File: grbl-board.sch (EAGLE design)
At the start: 20 parts, among them IC1 MEGA8-P, IC2 FT232RL, IC3 ADUM1250, Q1 16 MHz, X1 PN61729-S, X2 22-23-2031, X3 22-23-2031, X4 22-23-2031, X5 22-23-2021

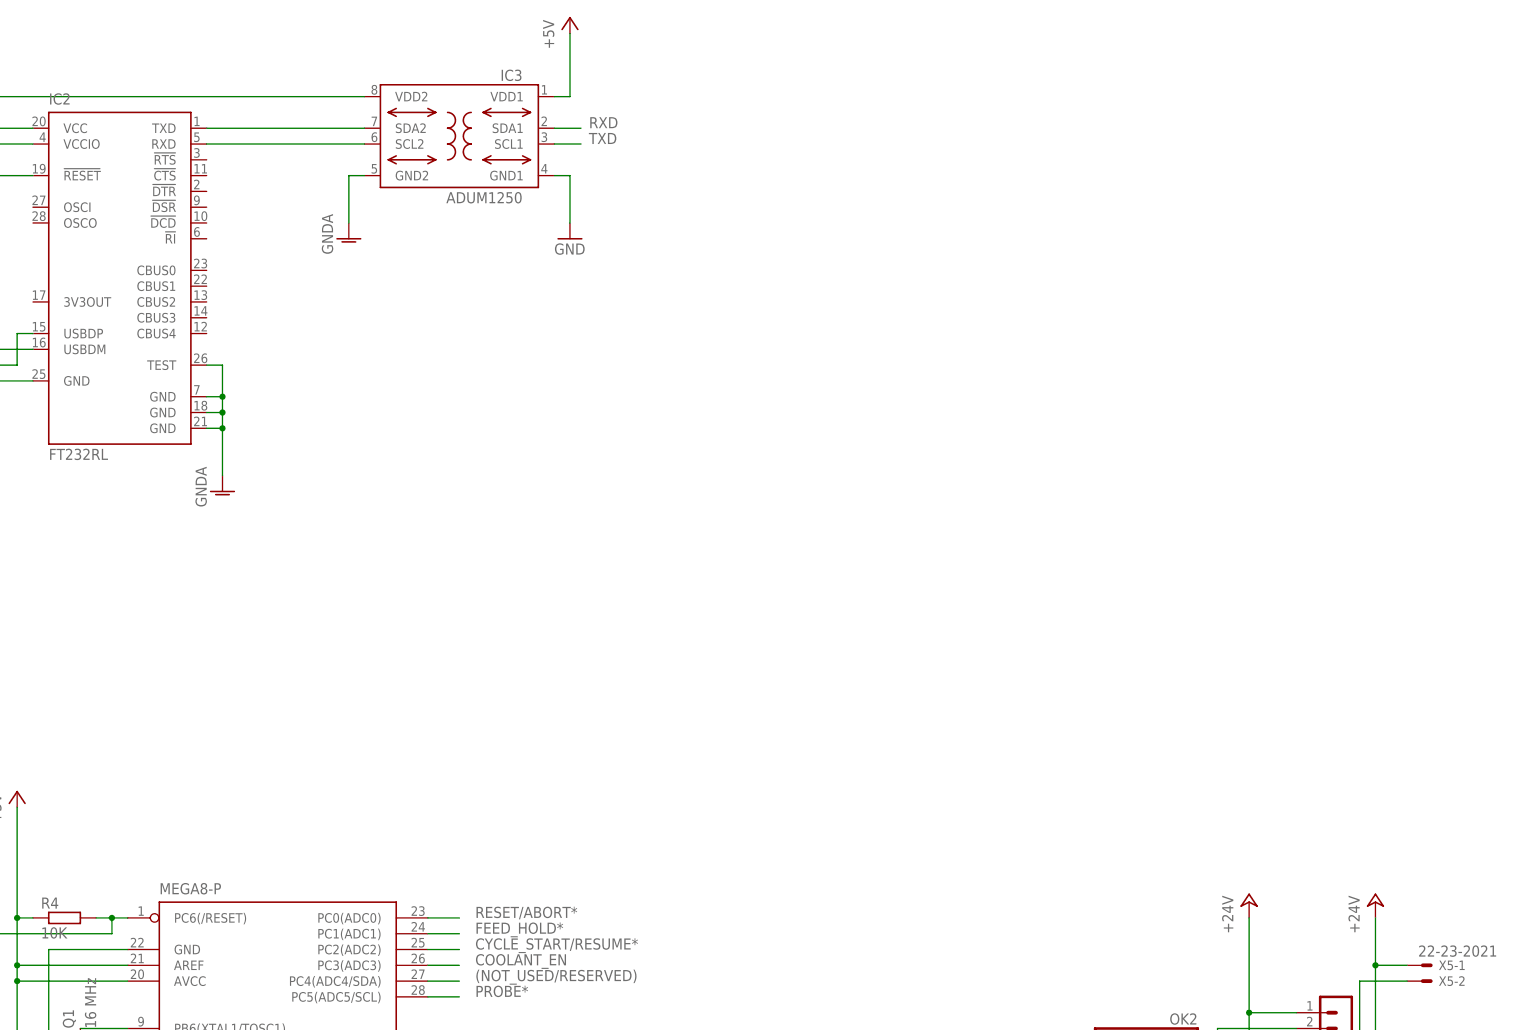
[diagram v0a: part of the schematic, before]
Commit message: add arduino nano2
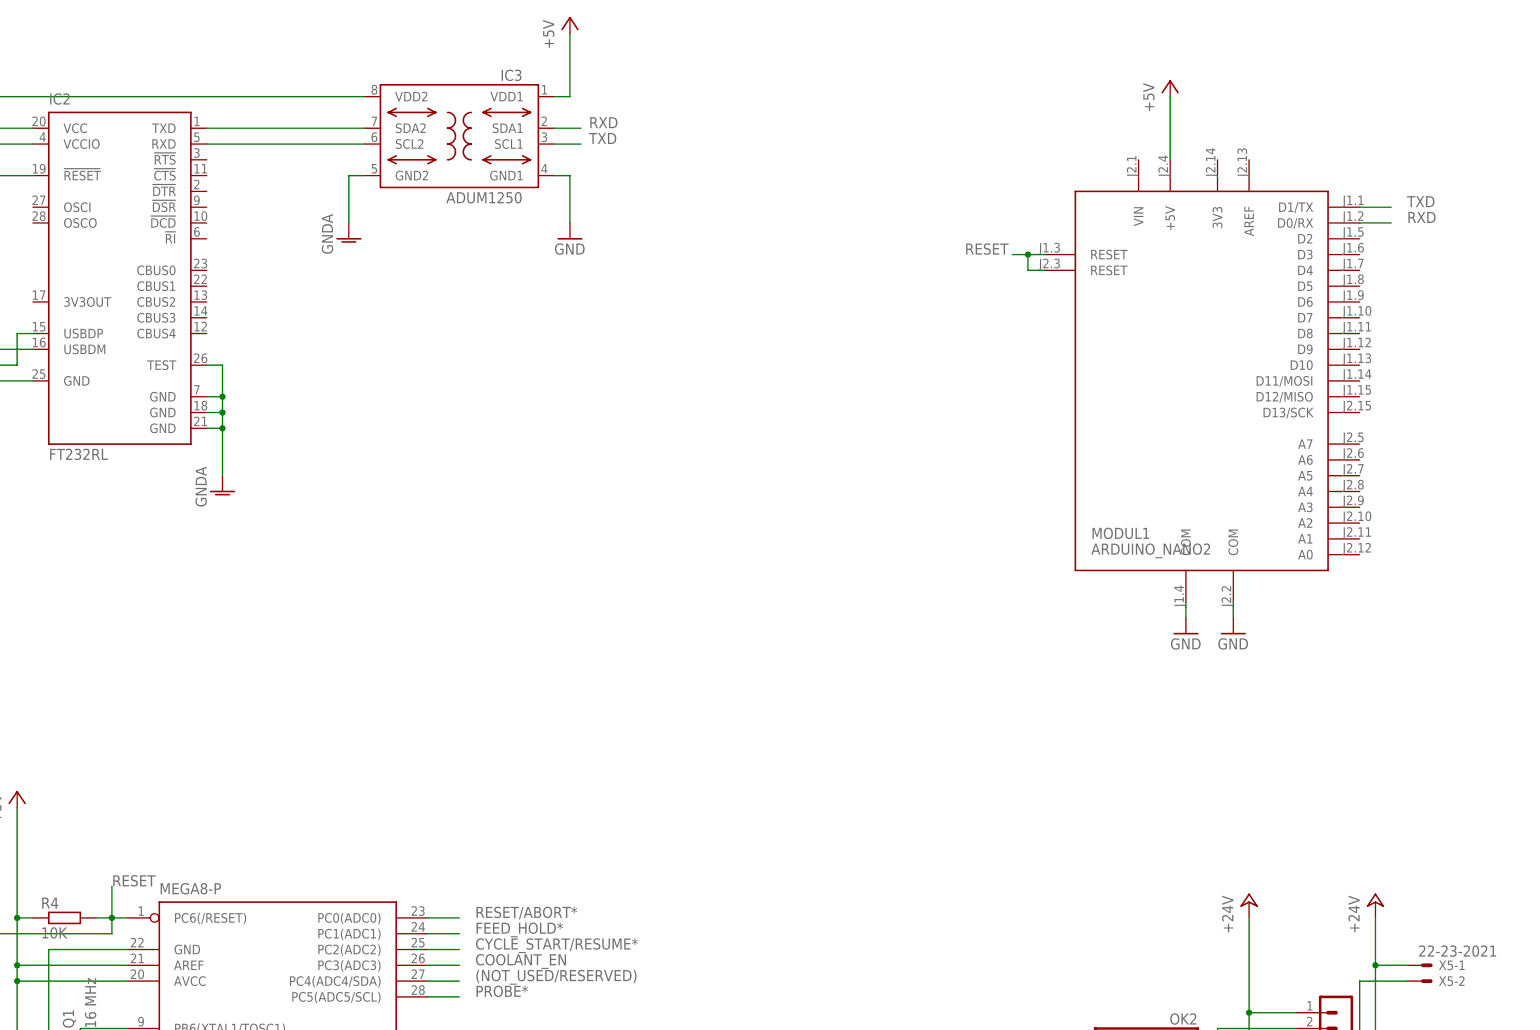
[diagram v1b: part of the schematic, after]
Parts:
- added MODUL1: ARDUINO_NANO2, arduino:ARDUINO_NANO2
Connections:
- removed net N$16: IC1.PC6(/RESET), R4.2, S1.S
- new net RESET: IC1.PC6(/RESET), MODUL1.RESET, MODUL1.RESET@2, R4.2, S1.S
- net +5V: now also MODUL1.+5V
- net GND: now also MODUL1.COM, MODUL1.COM@1
- net RXD: now also MODUL1.D0/RX
- net TXD: now also MODUL1.D1/TX
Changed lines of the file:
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@@
 <part name="S1" library="switch-omron" deviceset="10-XX" device=""/>
 <part name="GND7" library="supply1" deviceset="GND" device=""/>
+<part name="MODUL1" library="arduino" deviceset="ARDUINO_NANO2" device=""/>
+<part name="P+5" library="supply1" deviceset="+5V" device=""/>
+<part name="GND8" library="supply1" deviceset="GND" device=""/>
+<part name="GND9" library="supply1" deviceset="GND" device=""/>
 </parts>
 <sheets>
@@
 <instance part="S1" gate="1" x="81.28" y="91.44"/>
 <instance part="GND7" gate="1" x="81.28" y="53.34"/>
+<instance part="MODUL1" gate="MODUL" x="276.86" y="208.28"/>
+<instance part="P+5" gate="1" x="271.78" y="256.54"/>
+<instance part="GND8" gate="1" x="274.32" y="167.64"/>
+<instance part="GND9" gate="1" x="281.94" y="167.64"/>
 </instances>
 <busses>
@@
 <label x="160.02" y="99.06" size="1.778" layer="95"/>
 </segment>
+<segment>
+<pinref part="MODUL1" gate="MODUL" pin="D0/RX"/>
+<wire x1="302.26" y1="233.68" x2="307.34" y2="233.68" width="0.1524" layer="91"/>
+<label x="309.88" y="233.68" size="1.778" layer="95"/>
+</segment>
 </net>
 <net name="TXD" class="0">
@@
 <wire x1="152.4" y1="96.52" x2="157.48" y2="96.52" width="0.1524" layer="91"/>
 <label x="160.02" y="96.52" size="1.778" layer="95"/>
+</segment>
+<segment>
+<pinref part="MODUL1" gate="MODUL" pin="D1/TX"/>
+<wire x1="302.26" y1="236.22" x2="307.34" y2="236.22" width="0.1524" layer="91"/>
+<label x="309.88" y="236.22" size="1.778" layer="95"/>
 </segment>
 </net>
@@
 <wire x1="81.28" y1="86.36" x2="81.28" y2="55.88" width="0.1524" layer="91"/>
 <pinref part="GND7" gate="1" pin="GND"/>
+</segment>
+<segment>
+<pinref part="MODUL1" gate="MODUL" pin="COM"/>
+<wire x1="274.32" y1="172.72" x2="274.32" y2="170.18" width="0.1524" layer="91"/>
+<pinref part="GND8" gate="1" pin="GND"/>
+</segment>
+<segment>
+<pinref part="MODUL1" gate="MODUL" pin="COM@1"/>
+<wire x1="281.94" y1="172.72" x2="281.94" y2="170.18" width="0.1524" layer="91"/>
+<pinref part="GND9" gate="1" pin="GND"/>
 </segment>
 </net>
@@
 <junction x="86.36" y="121.92"/>
 </segment>
+<segment>
+<pinref part="MODUL1" gate="MODUL" pin="+5V"/>
+<pinref part="P+5" gate="1" pin="+5V"/>
+<wire x1="271.78" y1="243.84" x2="271.78" y2="254" width="0.1524" layer="91"/>
+</segment>
 </net>
 <net name="Z-LIMIT*" class="0">
@@
 </segment>
 </net>
-<net name="N$16" class="0">
+<net name="RESET" class="0">
+<segment>
+<pinref part="MODUL1" gate="MODUL" pin="RESET"/>
+<wire x1="251.46" y1="228.6" x2="248.92" y2="228.6" width="0.1524" layer="91"/>
+<pinref part="MODUL1" gate="MODUL" pin="RESET@2"/>
+<wire x1="248.92" y1="228.6" x2="246.38" y2="228.6" width="0.1524" layer="91"/>
+<wire x1="251.46" y1="226.06" x2="248.92" y2="226.06" width="0.1524" layer="91"/>
+<wire x1="248.92" y1="226.06" x2="248.92" y2="228.6" width="0.1524" layer="91"/>
+<junction x="248.92" y="228.6"/>
+<label x="238.76" y="228.6" size="1.778" layer="95"/>
+</segment>
 <segment>
 <pinref part="IC1" gate="G$1" pin="PC6(/RESET)"/>
@@
 <wire x1="81.28" y1="119.38" x2="81.28" y2="96.52" width="0.1524" layer="91"/>
 <junction x="101.6" y="121.92"/>
-</segment>
-</net>
+<label x="101.6" y="127" size="1.778" layer="95"/>
+<wire x1="101.6" y1="121.92" x2="101.6" y2="127" width="0.1524" layer="91"/>
+</segment>
+</net>

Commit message: add driver connectors
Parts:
- added X6, X7, X8: 22-23-2051, con-molex:22-23-2051
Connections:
- removed net STEPPER_ON/OFF: IC1.PB0(ICP)
- new net STEPPER_EN: IC1.PB0(ICP), MODUL1.D8, X6-5.S, X7-5.S, X8-5.S
- net (NOT_USED/RESERVED): now also MODUL1.A4
- net +5V: now also MODUL1.AREF, R4.2, X6-1.S, X7-1.S, X8-1.S; no longer R4.1
- net COOLANT_EN: now also MODUL1.A3
- net CYCLE_START/RESUME*: now also MODUL1.A2
- net FEED_HOLD*: now also MODUL1.A1
- net GND: now also X6-2.S, X7-2.S, X8-2.S
- net PROBE*: now also MODUL1.A5
- net RESET: now also R4.1; no longer R4.2
- net RESET/ABORT*: now also MODUL1.A0
- net SPINDLE-DIR: now also MODUL1.D13/SCK
- net SPINDLE-PWM: now also MODUL1.D11/MOSI
- net X-DIR: now also MODUL1.D5, X6-4.S
- net X-LIMIT*: now also MODUL1.D9
- net X-STEP: now also MODUL1.D2, X6-3.S
- net Y-DIR: now also MODUL1.D6, X7-4.S
- net Y-LIMIT*: now also MODUL1.D10
- net Y-STEP: now also MODUL1.D3, X7-3.S
- net Z-DIR: now also MODUL1.D7, X8-4.S
- net Z-LIMIT*: now also MODUL1.D12/MISO
- net Z-STEP: now also MODUL1.D4, X8-3.S
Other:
- moved on the sheet: OK1, OK2, OK3, Q1, R1, R2, R3, R4, S1, SV1, SV2, SV3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

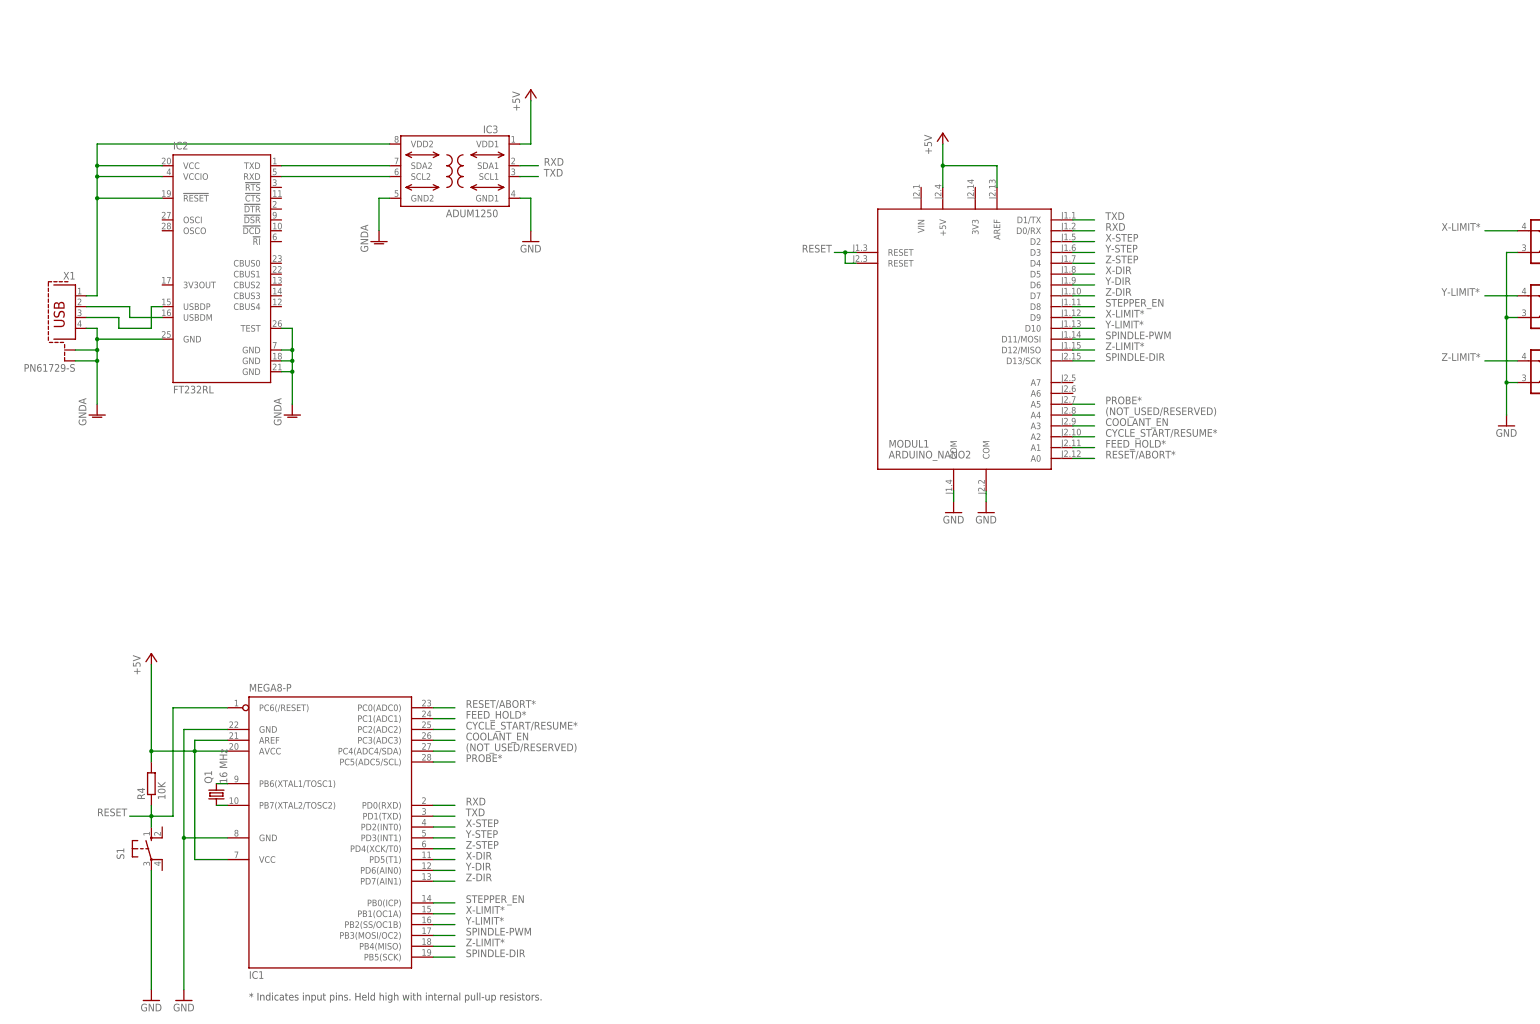
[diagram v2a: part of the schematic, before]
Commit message: add vreg add ISP
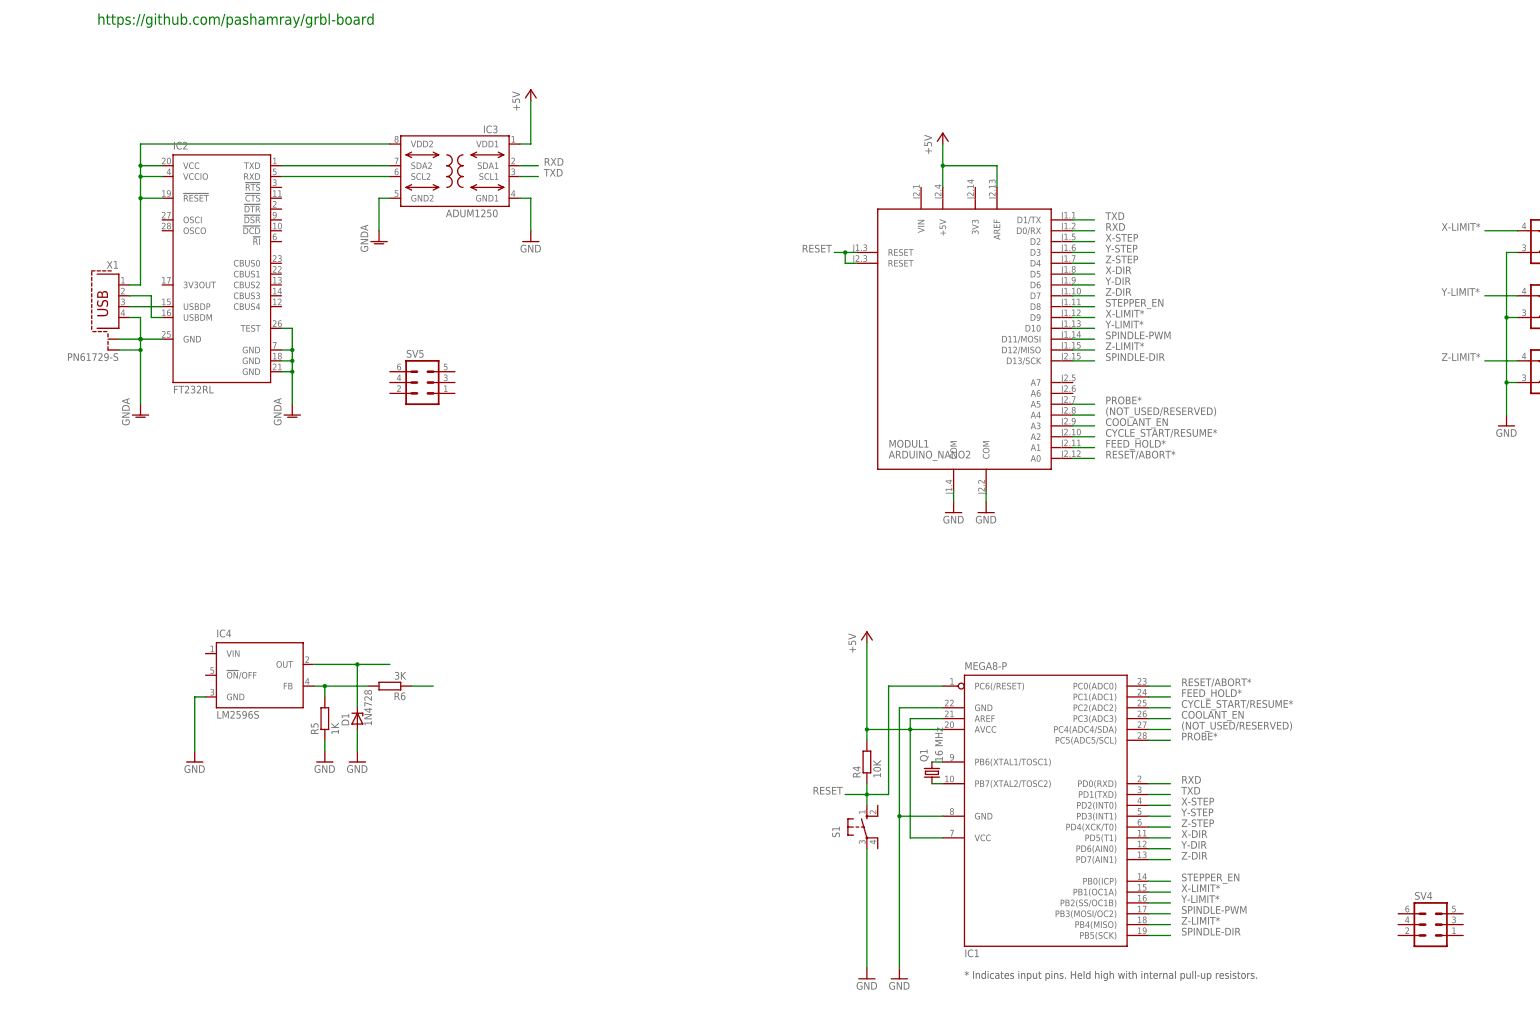
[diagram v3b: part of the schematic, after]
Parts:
- added D1: 1N4728, diode:1N4728
- added IC4: LM2596S, national-semiconductor:LM2596S
- added R5: 1K, resistor:R-EU_M0805
- added R6: 3K, resistor:R-EU_M0805
- added SV4, SV5: (no value), con-ml:ML6
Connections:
- new net N$16: D1.C, IC4.OUT
- new net N$17: R6.1
- new net N$18: IC4.FB, R5.2, R6.2
- net GND: now also D1.A, IC4.GND, R5.1
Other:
- note added: "https://github.com/pashamray/grbl-board"
- moved on the sheet: IC1, Q1, R4, S1, X1

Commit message: add arduino from adafruit library
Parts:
- removed MODUL1: ARDUINO_NANO2, arduino:ARDUINO_NANO2
- added C1: 100uF, adafruit:CPOL-USE5-13
- added C2: 1000uF, adafruit:CPOL-USE5-13
- added CN1: (no value), adafruit:DCBARRELPTH
- added L1: 100uH, adafruit:L1800R
- added U$1: ARDUINOMICRO, adafruit:ARDUINOMICRO
- D1: value 1N4728 -> 1N5822; device diode:1N4728 -> SwK-SparkFun:DIODE-SCHOTTKY_
- SV4: value (none) -> ISP
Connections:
- removed net N$17: R6.1
- new net N$19: C1.+, CN1.PWR, IC4.VIN
- net (NOT_USED/RESERVED): now also U$1.A4; no longer MODUL1.A4
- net +5V: now also C2.+, L1.1, R6.1, SV4.2, U$1.5V, U$1.AREF; no longer MODUL1.+5V, MODUL1.AREF
- net COOLANT_EN: now also U$1.A3; no longer MODUL1.A3
- net CYCLE_START/RESUME*: now also U$1.A2; no longer MODUL1.A2
- net FEED_HOLD*: now also U$1.A1; no longer MODUL1.A1
- net GND: now also C1.-, C2.-, CN1.GND, IC4.!ON!/OFF, SV4.6, U$1.GND, U$1.GND@1; no longer MODUL1.COM, MODUL1.COM@1
- net GNDA: now also SV5.6
- net N$16: now also L1.2
- net PROBE*: now also U$1.A5; no longer MODUL1.A5
- net RESET: now also SV4.5, U$1.R@1, U$1.R@2; no longer MODUL1.RESET, MODUL1.RESET@2
- net RESET/ABORT*: now also U$1.A0; no longer MODUL1.A0
- net RXD: now also U$1.RX; no longer MODUL1.D0/RX
- net SPINDLE-DIR: now also SV4.3, U$1.13; no longer MODUL1.D13/SCK
- net SPINDLE-PWM: now also SV4.4, U$1.11; no longer MODUL1.D11/MOSI
- net STEPPER_EN: now also U$1.8; no longer MODUL1.D8
- net TXD: now also U$1.TX; no longer MODUL1.D1/TX
- net X-DIR: now also U$1.5; no longer MODUL1.D5
- net X-LIMIT*: now also U$1.9; no longer MODUL1.D9
- net X-STEP: now also U$1.2; no longer MODUL1.D2
- net Y-DIR: now also U$1.6; no longer MODUL1.D6
- net Y-LIMIT*: now also U$1.10; no longer MODUL1.D10
- net Y-STEP: now also U$1.3; no longer MODUL1.D3
- net Z-DIR: now also U$1.7; no longer MODUL1.D7
- net Z-LIMIT*: now also SV4.1, U$1.12; no longer MODUL1.D12/MISO
- net Z-STEP: now also U$1.4; no longer MODUL1.D4
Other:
- moved on the sheet: IC1, IC4, OK1, OK2, OK3, Q1, R1, R2, R3, R4, R5, R6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

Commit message: add brd
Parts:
- removed IC1: MEGA8-P, atmel:MEGA8-P
- removed Q1: 16 MHz, crystal:CRYSTALHC49S
- removed R4: 10K, resistor:R-EU_M0805
- removed S1: (no value), switch-omron:10-XX
- removed SV5: (no value), con-ml:ML6
- removed X2, X3, X4: 22-23-2031, con-molex:22-23-2031
- removed X6, X7, X8: 22-23-2051, con-molex:22-23-2051
- added X-DRIVER, Y-DRIVER, Z-DRIVER: 22-23-2051, con-molex:22-23-2051
- added X-LIMIT, Y-LIMIT, Z-LIMIT: 22-23-2031, con-molex:22-23-2031
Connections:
- removed net N$6: IC1.PB6(XTAL1/TOSC1), Q1.2
- removed net N$7: IC1.PB7(XTAL2/TOSC2), Q1.1
- net (NOT_USED/RESERVED): no longer IC1.PC4(ADC4/SDA)
- net +24V: now also X-LIMIT-1.S, Y-LIMIT-1.S, Z-LIMIT-1.S; no longer X2-1.S, X3-1.S, X4-1.S
- net +5V: now also X-DRIVER-1.S, Y-DRIVER-1.S, Z-DRIVER-1.S; no longer IC1.AREF, IC1.AVCC, IC1.VCC@1, R4.2, X6-1.S, X7-1.S, X8-1.S
- net COOLANT_EN: no longer IC1.PC3(ADC3)
- net CYCLE_START/RESUME*: no longer IC1.PC2(ADC2)
- net DGND: now also X-LIMIT-3.S, Y-LIMIT-3.S, Z-LIMIT-3.S; no longer X2-3.S, X3-3.S, X4-3.S
- net FEED_HOLD*: no longer IC1.PC1(ADC1)
- net GND: now also X-DRIVER-2.S, Y-DRIVER-2.S, Z-DRIVER-2.S; no longer IC1.GND, IC1.GND@1, S1.P, X6-2.S, X7-2.S, X8-2.S
- net GNDA: no longer SV5.6
- net N$13: now also X-LIMIT-2.S; no longer X2-2.S
- net N$8: now also Y-LIMIT-2.S; no longer X3-2.S
- net N$9: now also Z-LIMIT-2.S; no longer X4-2.S
- net PROBE*: no longer IC1.PC5(ADC5/SCL)
- net RESET: no longer IC1.PC6(/RESET), R4.1, S1.S
- net RESET/ABORT*: no longer IC1.PC0(ADC0)
- net RXD: no longer IC1.PD0(RXD)
- net SPINDLE-DIR: no longer IC1.PB5(SCK)
- net SPINDLE-PWM: no longer IC1.PB3(MOSI/OC2)
- net STEPPER_EN: now also X-DRIVER-5.S, Y-DRIVER-5.S, Z-DRIVER-5.S; no longer IC1.PB0(ICP), X6-5.S, X7-5.S, X8-5.S
- net TXD: no longer IC1.PD1(TXD)
- net X-DIR: now also X-DRIVER-4.S; no longer IC1.PD5(T1), X6-4.S
- net X-LIMIT*: no longer IC1.PB1(OC1A)
- net X-STEP: now also X-DRIVER-3.S; no longer IC1.PD2(INT0), X6-3.S
- net Y-DIR: now also Y-DRIVER-4.S; no longer IC1.PD6(AIN0), X7-4.S
- net Y-LIMIT*: no longer IC1.PB2(SS/OC1B)
- net Y-STEP: now also Y-DRIVER-3.S; no longer IC1.PD3(INT1), X7-3.S
- net Z-DIR: now also Z-DRIVER-4.S; no longer IC1.PD7(AIN1), X8-4.S
- net Z-LIMIT*: no longer IC1.PB4(MISO)
- net Z-STEP: now also Z-DRIVER-3.S; no longer IC1.PD4(XCK/T0), X8-3.S
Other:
- note removed: "* Indicates input pins. Held high with internal pull-up resistors."
- moved on the sheet: C1, C2, CN1, D1, IC4, L1, OK1, OK2, OK3, R1, R2, R3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
